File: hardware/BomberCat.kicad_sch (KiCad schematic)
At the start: 86 parts, among them J1 Battery, J3 MAGSPOOF, P1 USB_C_Plug_USB2.0, Q1 DMG3415U-7, SW1 RESET, SW2 GPIO, SW3 ON, SW4 SOURCE MAG, U1 PN7150B0HN_C11002E-PN7150B0HN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, U2 RP2040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

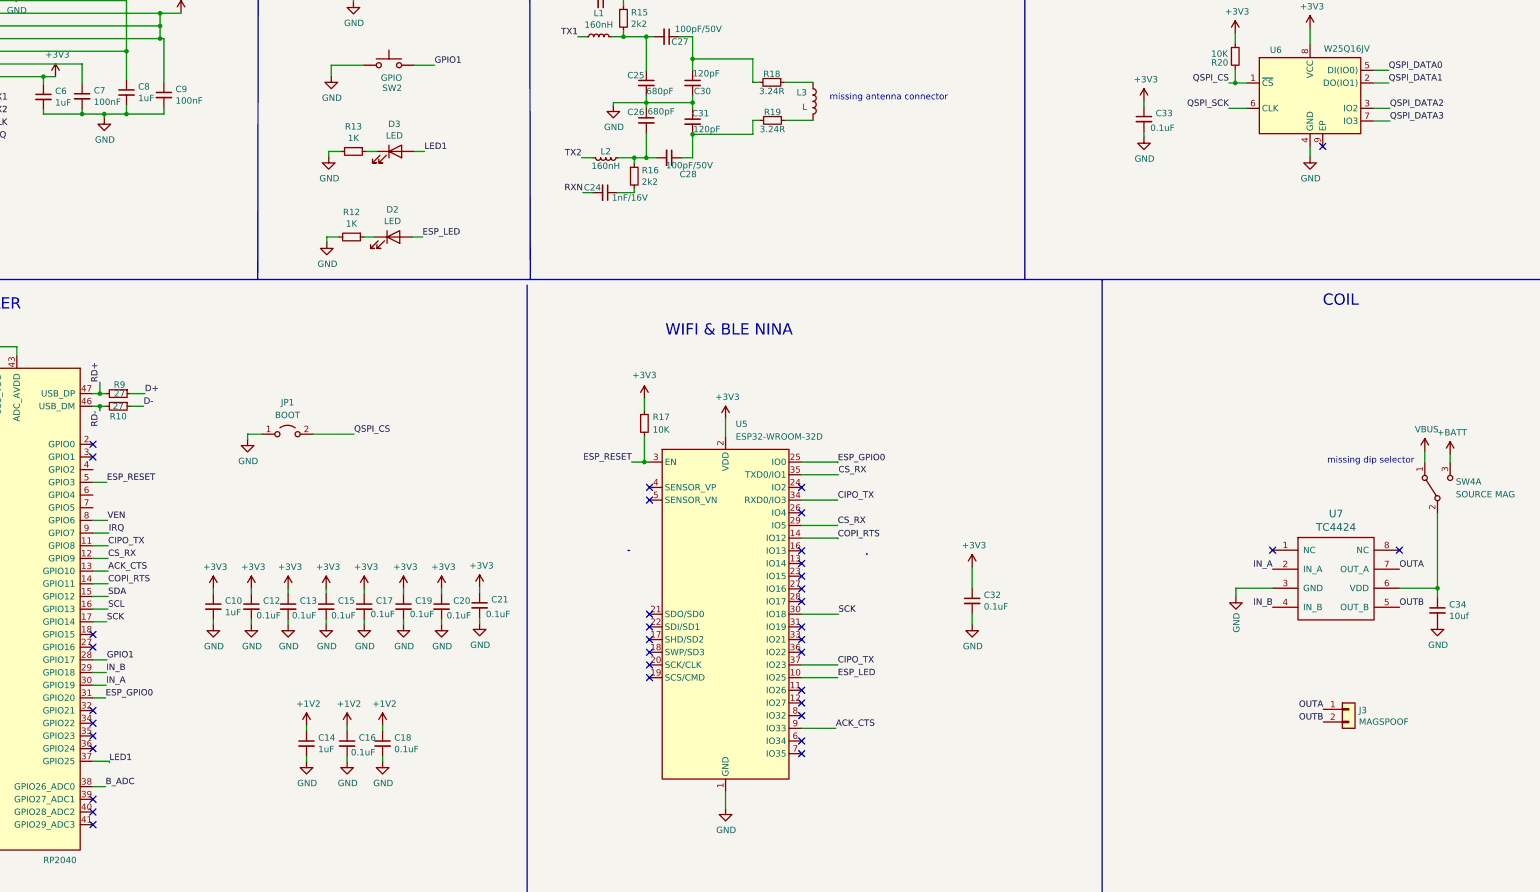
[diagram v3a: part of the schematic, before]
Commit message: layout update 0 unconnected added switchs
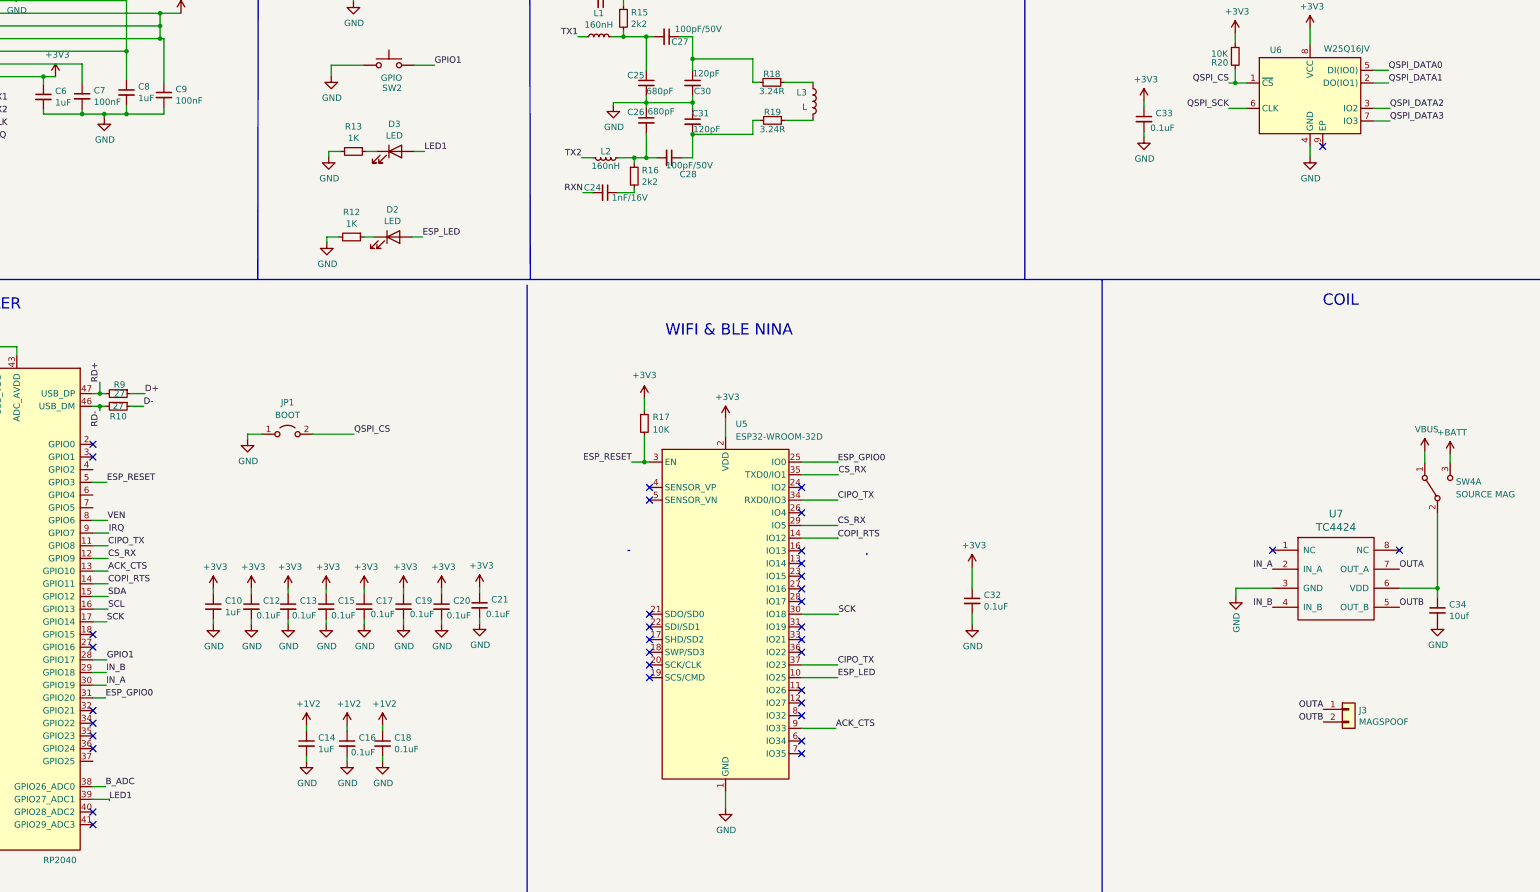
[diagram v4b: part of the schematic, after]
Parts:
- L3: footprint (none) -> Connectors:MOLEX_1661
- SW3: footprint RP2040:Micro_interruptor_SPDT -> BomberCat:JS102011SAQN; manf# - -> JS102011SAQN; provedor - -> MOUSER
- SW4: footprint (none) -> BomberCat:JS202011CQN; manf# (none) -> JS202011CQN; provedor (none) -> MOUSER
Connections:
- net LED1: now also U2.39 (GPIO27_ADC1); no longer U2.37 (GPIO25)
- no-connect marks 38 -> 37
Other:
- note removed: "missing antenna connector"
- note removed: "missing dip selector"
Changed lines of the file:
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@@
   (no_connect (at 111.76 195.58))
   (no_connect (at 111.76 193.04))
-  (no_connect (at 111.76 190.5))
   (wire (pts (xy 211.963 61.976) (xy 209.677 61.976))
     (stroke (width 0) (type default) (color 0 0 0 0))
@@
     (stroke (width 0) (type default) (color 0 0 0 0))
   )
-  (wire (pts (xy 111.76 182.88) (xy 115.062 182.88))
+  (wire (pts (xy 111.76 190.5) (xy 115.062 190.5))
     (stroke (width 0) (type default) (color 0 0 0 0))
   )
@@
     (stroke (width 0) (type default) (color 0 0 0 0))
   )
-  (wire (pts (xy 115.062 182.88) (xy 115.062 183.134))
+  (wire (pts (xy 115.062 190.5) (xy 115.062 190.754))
     (stroke (width 0) (type default) (color 0 0 0 0))
   )
@@
     (stroke (width 0) (type default) (color 0 0 0 0))
   )
-  (text "missing dip selector" (at 359.029 123.444 0)
-    (effects (font (size 1.27 1.27)) (justify left bottom))
-  )
-  (text "missing antenna connector\n" (at 259.334 50.673 0)
-    (effects (font (size 1.27 1.27)) (justify left bottom))
-  )
   (text "COIL" (at 358.14 91.948 0)
     (effects (font (size 2.2606 2.2606)) (justify left bottom))
@@
     (effects (font (size 1.27 1.27)) (justify right bottom))
   )
-  (label "LED1" (at 115.062 183.134 0)
+  (label "LED1" (at 115.062 190.754 0)
     (effects (font (size 1.27 1.27)) (justify left bottom))
   )
@@
       (effects (font (size 1.27 1.27)) (justify right))
     )
-    (property "Footprint" "" (id 2) (at 381.127 128.143 0)
+    (property "Footprint" "BomberCat:JS202011CQN" (id 2) (at 381.127 128.143 0)
+      (effects (font (size 1.27 1.27)) hide)
+    )
+    (property "Datasheet" "https://www.mouser.mx/datasheet/2/60/js-1841892.pdf" (id 3) (at 381.127 128.143 0)
+      (effects (font (size 1.27 1.27)) hide)
+    )
+    (property "manf#" "JS202011CQN" (id 4) (at 381.127 128.143 0)
       (effects (font (size 1.27 1.27)) hide)
     )
-    (property "Datasheet" "~" (id 3) (at 381.127 128.143 0)
+    (property "provedor" "MOUSER" (id 5) (at 381.127 128.143 0)
       (effects (font (size 1.27 1.27)) hide)
     )
@@
     (property "Reference" "SW3" (id 0) (at 197.485 253.492 0))
     (property "Value" "ON" (id 1) (at 197.485 247.8024 0))
-    (property "Footprint" "RP2040:Micro_interruptor_SPDT" (id 2) (at 197.485 251.46 0)
+    (property "Footprint" "BomberCat:JS102011SAQN" (id 2) (at 197.485 251.46 0)
       (effects (font (size 1.27 1.27)) hide)
     )
-    (property "Datasheet" "~" (id 3) (at 197.485 251.46 0)
+    (property "Datasheet" "https://www.mouser.mx/datasheet/2/60/js-1841892.pdf" (id 3) (at 197.485 251.46 0)
       (effects (font (size 1.27 1.27)) hide)
     )
@@
       (effects (font (size 1.27 1.27)) hide)
     )
-    (property "manf#" "-" (id 5) (at 197.485 251.46 0)
+    (property "manf#" "JS102011SAQN" (id 5) (at 197.485 251.46 0)
       (effects (font (size 1.27 1.27)) hide)
     )
-    (property "provedor" "-" (id 6) (at 197.485 251.46 0)
+    (property "provedor" "MOUSER" (id 6) (at 197.485 251.46 0)
       (effects (font (size 1.27 1.27)) hide)
     )
@@
       (effects (font (size 1.27 1.27)) (justify left))
     )
-    (property "Footprint" "" (id 2) (at 256.032 50.673 0)
+    (property "Footprint" "Connectors:MOLEX_1661" (id 2) (at 256.032 50.673 0)
       (effects (font (size 1.27 1.27)) hide)
     )
@@
     )
     (path "/987a4f27-e5bc-422b-abad-644d0bb5a08b"
-      (reference "L3") (unit 1) (value "L") (footprint "")
+      (reference "L3") (unit 1) (value "L") (footprint "Connectors:MOLEX_1661")
     )
     (path "/c398b8a2-afa6-42cd-ad50-5e6d204ddbd9"
@@
     )
     (path "/28eb8552-4fb1-41ec-b638-937731f8275e"
-      (reference "SW3") (unit 1) (value "ON") (footprint "RP2040:Micro_interruptor_SPDT")
+      (reference "SW3") (unit 1) (value "ON") (footprint "BomberCat:JS102011SAQN")
     )
     (path "/096a4d5f-6bcf-435a-be85-fcfb8aef10a7"
-      (reference "SW4") (unit 1) (value "SOURCE MAG") (footprint "")
+      (reference "SW4") (unit 1) (value "SOURCE MAG") (footprint "BomberCat:JS202011CQN")
     )
     (path "/b1a3604c-a799-4805-92d2-bea63c8fb54f"

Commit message: fix jumper for boot mode add 3Ds
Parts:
- JP1: footprint (none) -> Jumper:SolderJumper-2_P1.3mm_Open_TrianglePad1.0x1.5mm
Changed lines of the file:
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@@
     (property "Reference" "JP1" (id 0) (at 150.749 110.998 0))
     (property "Value" "BOOT" (id 1) (at 150.749 113.538 0))
-    (property "Footprint" "" (id 2) (at 150.749 117.348 0)
+    (property "Footprint" "Jumper:SolderJumper-2_P1.3mm_Open_TrianglePad1.0x1.5mm" (id 2) (at 150.749 117.348 0)
       (effects (font (size 1.27 1.27)) hide)
     )
@@
     )
     (path "/ae267929-5045-405c-9bb8-319a56701526"
-      (reference "JP1") (unit 1) (value "BOOT") (footprint "")
+      (reference "JP1") (unit 1) (value "BOOT") (footprint "Jumper:SolderJumper-2_P1.3mm_Open_TrianglePad1.0x1.5mm")
     )
     (path "/9a537aef-6cf7-41cb-9cbc-80e780f89c6e"

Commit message: update BOM
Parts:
- C10, C14: LCSC# (none) -> C26413; manf# EC -> 885012207078; provedor (none) -> LCSC
- C12, C13, C15, C16, C17, C18, C19, C20, C21, C33: LCSC# (none) -> C387984; manf# EC -> -; provedor (none) -> LCSC
- C32: manf# 885012207072 -> -
- P1: LCSC# C393939 -> C2987386
- R10, R9: provedor (none) -> LCSC
- R17, R20: LCSC# (none) -> C15401; manf# (none) -> -; provedor (none) -> LCSC
- R3: LCSC# (none) -> C517454; manf# (none) -> CRCW08051K50FKEAC; provedor (none) -> LCSC
- U6: provedor (none) -> MOUSER

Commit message: Add_BOM
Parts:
- C1, C2: LCSC# (none) -> C880634; manf# EC -> TCC0603COG270J101CT; provedor (none) -> LCSC
- C10, C14, C5, C6, C8: LCSC# C26413 -> C15849; manf# 885012207078 -> CL10A105KB8NNNC
- C11, C22, C29: LCSC# C326057 -> C85713; manf# C0805C106K9PACTU -> CL10A106MP8NNNC
- C12, C13, C15, C16, C17, C18, C19, C20, C21, C32, C33: LCSC# C387984 -> C376764; manf# - -> TCC0603COG100J500CT
- C3, C4: LCSC# (none) -> C376764; manf# 885012007076 -> TCC0603COG100J500CT
- C30, C31: LCSC# (none) -> C561174; manf# C0603C121J5GAC -> C1608NP0121JGTS
- C34: LCSC# (none) -> C466781; manf# (none) -> C0603X5R106M160NT; provedor (none) -> LCSC
- C7, C9: LCSC# C387984 -> C235731; manf# 885012207072 -> FN18X104K500PBG
- D1: LCSC# C205441 -> C965815; manf# - -> XL-2012UGC
- D2, D3: LCSC# C130114 -> C965815; manf# - -> XL-2012UGC
- D4: LCSC# C723989 -> C130880; manf# - -> MBR120LSF
- P1: LCSC# C2987386 -> C2760486; manf# - -> TYPE-C-31-M-31
- Q1: manf# - -> DMG3415U-7
- R1, R17, R2, R20: LCSC# C15401 -> C169849; manf# - -> ERJ3GEYJ103V
- R10, R9: LCSC# (none) -> C403464; manf# (none) -> ERJ3GEYJ270V
- R11, R12, R13, R3, R8: LCSC# C517454 -> C112433; manf# CRCW08051K50FKEAC -> WR06X1001FTL
- R14, R21, R22, R6, R7: LCSC# C15458 -> C163843; manf# ERJ6RBD1003V -> WR06X104JTL
- R15, R16: LCSC# C217937 -> C113303
- R18, R19: LCSC# (none) -> C482832; provedor MOUSER -> LCSC
- R4, R5: LCSC# C131715 -> C191782; manf# CR0805-FX-5101ELF -> ERJ3RBD5101V
- SW1, SW2: LCSC# C318890 -> C2886897; manf# - -> TL3342F450QG
- U1: LCSC# - -> C11002; manf# PN7150B0HN/C11002 -> PN7150B0HN
- U2: LCSC# (none) -> C2040; manf# (none) -> RP2040; provedor (none) -> LCSC
- U5: LCSC# (none) -> C473012; manf# (none) -> ESP32-WROOM-32D; provedor (none) -> LCSC
- U7: LCSC# (none) -> C636876; manf# (none) -> TC4424AVOA
- Y1: LCSC# - -> C910048; manf# 520-271.2-6-37-JTNT -> NX2016SA-27.12MHZ-STD-CZS-3; provedor MOUSER -> LCSC
- Y2: LCSC# (none) -> C3035208; manf# ECS-120-18-30-JGN-TR -> SX5A12.000F2010F30; provedor MOUSER -> LCSC

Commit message: Update_BOM
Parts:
- C1, C2: LCSC# C880634 -> C92670; manf# TCC0603COG270J101CT -> 0603CG270J500NT
- C3, C4: LCSC# C376764 -> C106245; manf# TCC0603COG100J500CT -> CC0603JRNPO9BN100
- C7, C9: LCSC# C235731 -> (none); manf# FN18X104K500PBG -> (none)
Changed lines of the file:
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@@
       (effects (font (size 1.27 1.27)) hide)
     )
-    (property "manf#" "TCC0603COG100J500CT" (id 4) (at 36.83 66.929 0)
+    (property "manf#" "CC0603JRNPO9BN100" (id 4) (at 36.83 66.929 0)
       (effects (font (size 1.27 1.27)) hide)
     )
@@
       (effects (font (size 1.27 1.27)) hide)
     )
-    (property "LCSC#" "C376764" (id 6) (at 36.83 66.929 0)
+    (property "LCSC#" "C106245" (id 6) (at 36.83 66.929 0)
       (effects (font (size 1.27 1.27)) hide)
     )
@@
       (effects (font (size 1.27 1.27)) hide)
     )
-    (property "manf#" "FN18X104K500PBG" (id 4) (at 125.984 49.403 0)
+    (property "manf#" "" (id 4) (at 125.984 49.403 0)
       (effects (font (size 1.27 1.27)) hide)
     )
@@
       (effects (font (size 1.27 1.27)) hide)
     )
-    (property "LCSC#" "C235731" (id 6) (at 125.984 49.403 0)
+    (property "LCSC#" "" (id 6) (at 125.984 49.403 0)
       (effects (font (size 1.27 1.27)) hide)
     )
@@
       (effects (font (size 1.27 1.27)) hide)
     )
-    (property "LCSC#" "C880634" (id 4) (at 20.955 169.164 0)
-      (effects (font (size 1.27 1.27)) hide)
-    )
-    (property "manf#" "TCC0603COG270J101CT" (id 5) (at 20.955 169.164 0)
+    (property "LCSC#" "C92670" (id 4) (at 20.955 169.164 0)
+      (effects (font (size 1.27 1.27)) hide)
+    )
+    (property "manf#" "0603CG270J500NT" (id 5) (at 20.955 169.164 0)
       (effects (font (size 1.27 1.27)) hide)
     )
@@
       (effects (font (size 1.27 1.27)) hide)
     )
-    (property "manf#" "TCC0603COG100J500CT" (id 4) (at 42.164 67.056 0)
+    (property "manf#" "CC0603JRNPO9BN100" (id 4) (at 42.164 67.056 0)
       (effects (font (size 1.27 1.27)) hide)
     )
@@
       (effects (font (size 1.27 1.27)) hide)
     )
-    (property "LCSC#" "C376764" (id 6) (at 42.164 67.056 0)
+    (property "LCSC#" "C106245" (id 6) (at 42.164 67.056 0)
       (effects (font (size 1.27 1.27)) hide)
     )
@@
       (effects (font (size 1.27 1.27)) hide)
     )
-    (property "manf#" "FN18X104K500PBG" (id 4) (at 109.601 49.657 0)
+    (property "manf#" "" (id 4) (at 109.601 49.657 0)
       (effects (font (size 1.27 1.27)) hide)
     )
@@
       (effects (font (size 1.27 1.27)) hide)
     )
-    (property "LCSC#" "C235731" (id 6) (at 109.601 49.657 0)
+    (property "LCSC#" "" (id 6) (at 109.601 49.657 0)
       (effects (font (size 1.27 1.27)) hide)
     )
@@
       (effects (font (size 1.27 1.27)) hide)
     )
-    (property "LCSC#" "C880634" (id 4) (at 33.655 169.799 0)
-      (effects (font (size 1.27 1.27)) hide)
-    )
-    (property "manf#" "TCC0603COG270J101CT" (id 5) (at 33.655 169.799 0)
-      (effects (font (size 1.27 1.27)) hide)
-    )
+    (property "LCSC#" "C92670" (id 4) (at 33.655 169.799 0)
+      (effects (font (size 1.27 1.27)) hide)
+    )
+    (property "manf#" "0603CG270J500NT" (id 5) (at 33.655 169.799 0)
+      (effects (font (size 1.27 1.27)) hide)
+    )
